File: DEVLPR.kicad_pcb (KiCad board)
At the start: 2 copper layers, 68.6 x 53.3 mm, 56 parts, among them CON1 3.5mm EMG, J1 EMG OUTPUT, P1 Power, P2 Analog, P3 Digital, P4 Digital, P5 CONN_01X01, P6 CONN_01X01, P7 CONN_01X01, P8 CONN_01X01, U1 TPS60402, U2 MAX1735, U3 OPA375DCK, U4 INA819IDGK, U5 OPA376xxD, U6 OPA376xxD

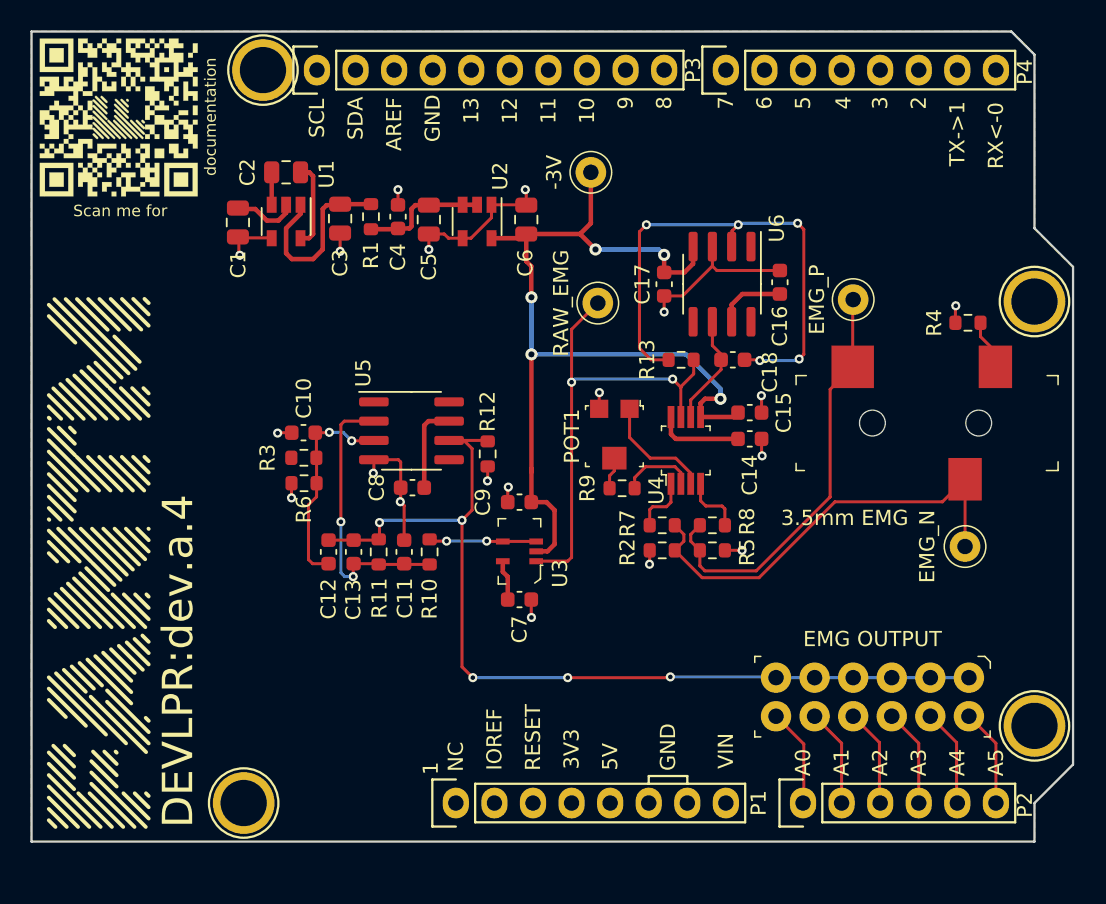
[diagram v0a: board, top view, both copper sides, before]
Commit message: Created v1.1 of the DEVLPR, adding RLD
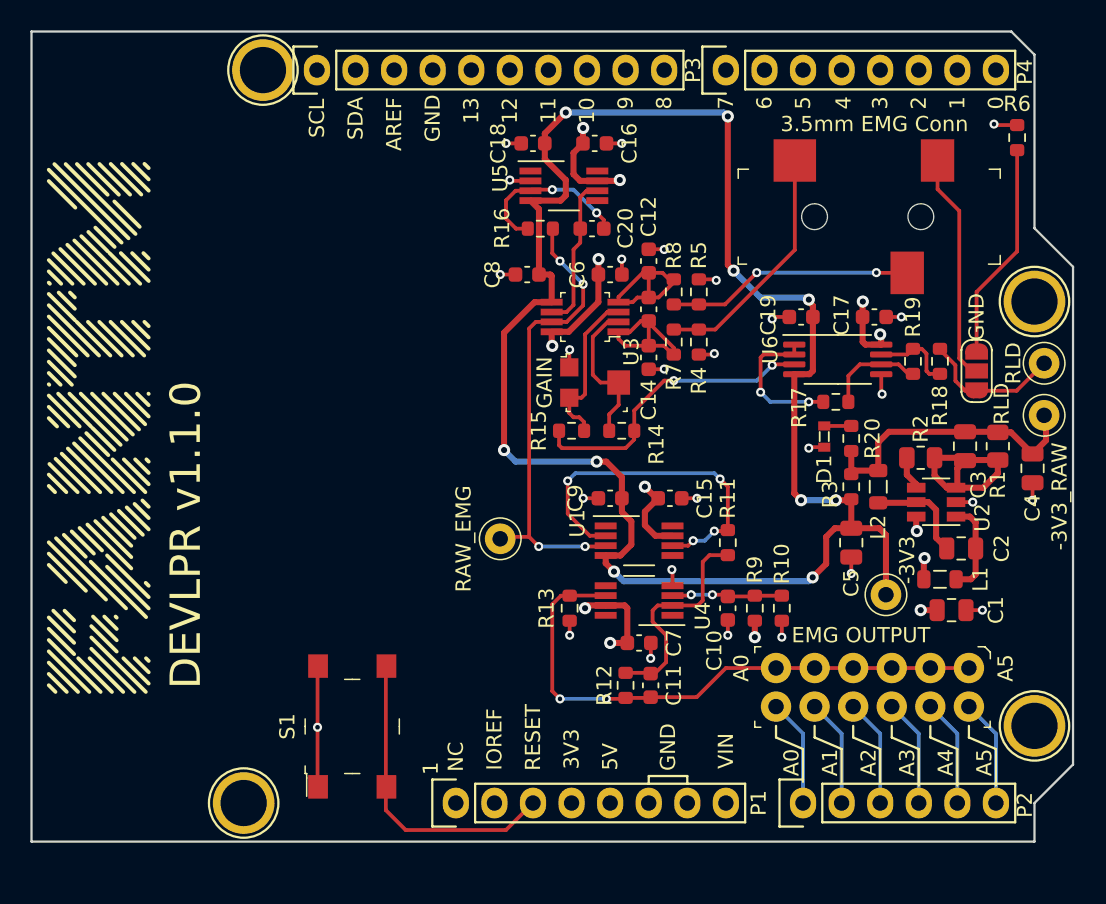
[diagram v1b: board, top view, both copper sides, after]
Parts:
- removed the C11 at (135.5, 107.3)
- removed the C6 at (143.6, 85.4)
- removed the C8 at (136.1, 103.1)
- removed G***: LOGO, kicad:oh_norm
- removed G***: LOGO, kicad:cc_reg
- removed G***: LOGO, kicad:logo
- removed the R4 at (172.7, 92.2)
- removed REF**: KiCad-Logo2_5mm_SilkScreen, Symbol:KiCad-Logo2_5mm_SilkScreen
- added C13: 10pF, Capacitor_SMD:C_0603_1608Metric, F.Cu at (151.6, 91.3)
- added C14: 2.2pF, Capacitor_SMD:C_0603_1608Metric, F.Cu at (151.6, 94.5)
- added C15: 0.1uF, Capacitor_SMD:C_0603_1608Metric, F.Cu at (153.0, 103.8)
- added C16: 0.1uF, Capacitor_SMD:C_0603_1608Metric, F.Cu at (148.1, 80.4)
- added C18: 0.1uF, Capacitor_SMD:C_0603_1608Metric, F.Cu at (144.0, 80.4)
- added D1: GREEN LED, digikey-footprints:0603, F.Cu at (163.2, 99.7)
- added JP1: RLD_SEL, Jumper:SolderJumper-3_P1.3mm_Open_RoundedPad1.0x1.5mm_NumberLabels, F.Cu at (173.2, 95.4)
- added L1: 10uH, Inductor_SMD:L_0805_2012Metric, F.Cu at (170.8, 109.1)
- added L2: 10uH, Inductor_SMD:L_0805_2012Metric, F.Cu at (166.8, 103.0)
- added R11: 10k, Resistor_SMD:R_0603_1608Metric, F.Cu at (156.8, 106.7)
- added R15: 470, Resistor_SMD:R_0603_1608Metric, F.Cu at (146.6, 99.3)
- added R17: 10k, Resistor_SMD:R_0603_1608Metric, F.Cu at (164.0, 97.4)
- added R18: 100k, Resistor_SMD:R_0603_1608Metric, F.Cu at (170.8, 94.7)
- added R19: 100k, Resistor_SMD:R_0603_1608Metric, F.Cu at (169.0, 94.7)
- added R2: 102k, Resistor_SMD:R_0805_2012Metric, F.Cu at (169.5, 101.1)
- added R20: 1k, Resistor_SMD:R_0603_1608Metric, F.Cu at (165.0, 99.8)
- added R3: 249, Resistor_SMD:R_0603_1608Metric, F.Cu at (165.0, 103.0)
- added S1: PTS645SM43SMTR92_LFS, digikey-footprints:Switch_Tactile_SMD_6x6mm_PTS645, F.Cu at (132.1, 118.8)
- added S2: Linus, FANTM:linus_xsm, B.Cu at (171.8, 109.0)
- added S3: Sinclair, FANTM:sin_ham_bitmap_sm, B.Cu at (172.9, 101.8)
- added S4: Kicad, Symbol:KiCad-Logo2_5mm_SilkScreen, B.Cu at (171.4, 84.3)
- added S5: OSHW, Symbol:OSHW-Symbol_6.7x6mm_SilkScreen, B.Cu at (171.4, 94.4)
- added S6: Portrait, FANTM:portait, B.Cu at (136.5, 80.9)
- added S7: Name, FANTM:name, B.Cu at (133.1, 116.0)
- C1, C2: value 3.3uF -> 1uF
- C12: value 4700pF -> 2.2pF
- C3: value 3.3uF -> 22pF
- C4: value 0.1uF -> 4.7uF; footprint Capacitor_SMD:C_0603_1608Metric -> Capacitor_SMD:C_0805_2012Metric
- C5: value 1uF -> 10uF
- CON1: value 3.5mm EMG -> SJ-3523-SMT-TR
- R1: value 249 -> 267k; footprint Resistor_SMD:R_0603_1608Metric -> Resistor_SMD:R_0805_2012Metric
- R10: value 3.3k -> 10k
- R12: renamed from R11; value 69.8k -> 28.7k
- R6: value 1k -> 100k
- R9: renamed from R3; value 43.2k -> 68k
- TP1: value EMG_N -> -3V3_RAW
- TP2: value EMG_P -> -3V3
- TP3: value -3V -> RAW_EMG
- TP4: value RAW_EMG -> RLD
- U1: value TPS60402 -> OPA187IDR; footprint Package_TO_SOT_SMD:SOT-23-5 -> Package_SO:VSSOP-8_3.0x3.0mm_P0.65mm
- U2: value MAX1735 -> LT3462A; footprint Package_TO_SOT_SMD:SOT-23-5 -> Package_TO_SOT_SMD:TSOT-23-6
- U3: value OPA375DCK -> INA821IDGKT; footprint digikey-footprints:SC-70-5 -> digikey-footprints:TSSOP-8_W3mm
- U4: value INA819IDGK -> OPA187IDR; footprint digikey-footprints:TSSOP-8_W3mm -> Package_SO:VSSOP-8_3.0x3.0mm_P0.65mm
- U5: value OPA376xxD -> OPA187IDR; footprint Package_SO:SOIC-8_3.9x4.9mm_P1.27mm -> Package_SO:VSSOP-8_3.0x3.0mm_P0.65mm
- U6: value OPA376xxD -> OPA2375IPWR; footprint Package_SO:SOIC-8_3.9x4.9mm_P1.27mm -> Package_SO:TSSOP-8_4.4x3mm_P0.65mm
- moved C1 53.5 mm to (171.6, 111.1), turned to 0 degrees
- moved R6 52.2 mm to (175.9, 80.0), turned to 90 degrees
- moved C2 50.9 mm to (172.2, 107.1)
- moved C4 44.9 mm to (176.9, 101.8)
- moved R1 44.0 mm to (174.6, 100.3), turned to 270 degrees
- moved C3 43.8 mm to (172.5, 100.3), turned to 270 degrees
- moved U2 35.4 mm to (170.6, 104.0), turned to 180 degrees
- moved C5 35.0 mm to (165.0, 106.7), turned to 270 degrees
- moved U1 31.3 mm to (151.0, 106.6), turned to 0 degrees
- moved R9 31.3 mm to (158.6, 111.0), turned to 90 degrees
- moved C10 30.2 mm to (156.8, 111.0), turned to 90 degrees
- moved TP4 29.7 mm to (177.7, 94.9)
- moved C12 28.5 mm to (151.6, 88.1)
- moved TP3 24.9 mm to (141.9, 106.4)
- moved R10 23.5 mm to (160.4, 111.0), turned to 270 degrees
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- renumbered C13 to C11, C16 to C17, C17 to C19, C18 to C20, C14 to C6, C15 to C8, R12 to R13, R9 to R14, R13 to R16, R2 to R4
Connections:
- C1 pad 1: GND -> +3V3
- C1 pad 2: +5V -> GND
- C11 pad 1: /EMG Amplifiers/BUFFER_OUT -> /EMG Amplifiers/BUFF_MID
- C12 pad 1: /EMG Amplifiers/V_SHIFT -> /EMG Amplifiers/INA_P
- C12 pad 2: /EMG_OUT -> GND
- C17 pad 2: +5V -> +3V3
- C19 pad 2: -3V -> -3V3
- C2 pad 1: /-5V Source/Cfly- -> /-3V3 Source/-3V3_D
- C2 pad 2: /-5V Source/Cfly+ -> /-3V3 Source/-3V3_SW
- C3 pad 1: GND -> /-3V3 Source/-3V3_RAW
- C3 pad 2: /-5V Source/INV_OUT -> /-3V3 Source/-3V3_FB
- C4 pad 1: GND -> /-3V3 Source/-3V3_RAW
- C4 pad 2: /-5V Source/LDO_IN -> GND
- C5 pad 1: GND -> -3V3
- C5 pad 2: /-5V Source/LDO_IN -> GND
- C6 pad 2: +5V -> +3V3
- C7 pad 2: +5V -> +3V3
- C8 pad 2: -3V -> -3V3
- C9 pad 2: -3V -> -3V3
- CON1 pad 2: /EMG_P -> /EMG_N
- CON1 pad 3: /EMG_N -> /EMG_P
- P1 pad 1: Net-(P1-Pad1) -> (no net)
- P1 pad 2: /IOREF -> (no net)
- P1 pad 5: +5V -> (no net)
- P1 pad 8: /Vin -> (no net)
- P3 pad 1: /SCL -> (no net)
- P3 pad 10: /8 -> (no net)
- P3 pad 2: /SDA -> (no net)
- P3 pad 3: /AREF -> (no net)
- P3 pad 5: /13(SCK) -> (no net)
- P3 pad 6: /12(SDI) -> (no net)
- P3 pad 7: /11(**|SDO) -> (no net)
- P3 pad 8: /10(**|CS) -> (no net)
- P3 pad 9: /9(**) -> (no net)
- P4 pad 1: /7 -> (no net)
- P4 pad 2: /6(**) -> (no net)
- P4 pad 3: /5(**) -> (no net)
- P4 pad 4: /4 -> (no net)
- P4 pad 5: /3(**) -> (no net)
- P4 pad 6: /2 -> (no net)
- P4 pad 7: /1(Tx) -> (no net)
- P4 pad 8: /0(Rx) -> (no net)
- P5 pad 1: Net-(P5-Pad1) -> (no net)
- P6 pad 1: Net-(P6-Pad1) -> (no net)
- P7 pad 1: Net-(P7-Pad1) -> (no net)
- P8 pad 1: Net-(P8-Pad1) -> (no net)
- POT1 pad 1: /EMG Amplifiers/RG_2 -> GND
- POT1 pad 2: Net-(POT1-Pad2) -> /EMG Amplifiers/RG1
- POT1 pad 3: GND -> /EMG Amplifiers/RG2
- R1 pad 1: /-5V Source/LDO_IN -> /-3V3 Source/-3V3_RAW
- R1 pad 2: /-5V Source/INV_OUT -> /-3V3 Source/-3V3_FB
- R10 pad 1: /EMG Amplifiers/BUFFER_OUT -> /EMG Amplifiers/V_SHIFT
- R10 pad 2: /EMG Amplifiers/BUFFER_FDBK -> GND
- R12 pad 2: /EMG Amplifiers/BUFFER_OUT -> /EMG Amplifiers/BUFF_MID
- R14 pad 1: Net-(POT1-Pad2) -> /EMG Amplifiers/RLD_IN
- R14 pad 2: /EMG Amplifiers/RG_1 -> /EMG Amplifiers/RG1
- R6 pad 1: /EMG Amplifiers/V_SHIFT -> /EMG Amplifiers/GND_REF
- R9 pad 1: +5V -> +3V3
- TP1 pad 1: /EMG_N -> /-3V3 Source/-3V3_RAW
- TP2 pad 1: /EMG_P -> -3V3
- TP3 pad 1: -3V -> /EMG Amplifiers/EMG_INSTR
- TP4 pad 1: /EMG Amplifiers/EMG_INSTR -> /EMG Amplifiers/RLD
- U1 pad 1: /-5V Source/INV_OUT -> (no net)
- U1 pad 2: +5V -> /EMG Amplifiers/BUFF_FDBK
- U1 pad 3: /-5V Source/Cfly- -> /EMG Amplifiers/EMG_INSTR
- U1 pad 4: GND -> -3V3
- U1 pad 5: /-5V Source/Cfly+ -> (no net)
- U2 pad 1: GND -> /-3V3 Source/-3V3_SW
- U2 pad 2: /-5V Source/LDO_IN -> GND
- U2 pad 3: /-5V Source/LDO_IN -> /-3V3 Source/-3V3_FB
- U2 pad 4: GND -> /-3V3 Source/-3V3_SDREF
- U2 pad 5: -3V -> /-3V3 Source/-3V3_D
- U3 pad 1: /EMG Amplifiers/EMG_INSTR -> /EMG Amplifiers/INA_N
- U3 pad 2: -3V -> /EMG Amplifiers/RG1
- U3 pad 3: /EMG Amplifiers/BUFFER_FDBK -> /EMG Amplifiers/RG2
- U3 pad 4: /EMG Amplifiers/BUFFER_FDBK -> /EMG Amplifiers/INA_P
- U3 pad 5: +5V -> -3V3
- U4 pad 1: /EMG Amplifiers/INA_N -> (no net)
- U4 pad 2: /EMG Amplifiers/RG_1 -> /EMG Amplifiers/BUFF_MID
- U4 pad 3: /EMG Amplifiers/RG_2 -> /EMG Amplifiers/V_SHIFT
- U4 pad 4: /EMG Amplifiers/INA_P -> GND
- U4 pad 5: -3V -> (no net)
- U4 pad 6: /EMG Amplifiers/INA_REF -> /EMG_OUT
- U4 pad 7: /EMG Amplifiers/EMG_INSTR -> +3V3
- U4 pad 8: +5V -> (no net)
- U5 pad 1: Net-(U5-Pad1) -> (no net)
- U5 pad 2: /EMG Amplifiers/BUFFER_OUT -> GND
- U5 pad 3: /EMG Amplifiers/V_SHIFT -> /EMG Amplifiers/REF_-
- U5 pad 4: GND -> -3V3
- U5 pad 5: Net-(U5-Pad5) -> (no net)
- U5 pad 6: /EMG_OUT -> /EMG Amplifiers/INA_REF
- U5 pad 7: +5V -> +3V3
- U5 pad 8: Net-(U5-Pad8) -> (no net)
- U6 pad 1: Net-(U6-Pad1) -> /EMG Amplifiers/RLD_MID
- U6 pad 2: /EMG Amplifiers/REF_- -> /EMG Amplifiers/RLD_MID
- U6 pad 3: GND -> /EMG Amplifiers/RLD_IN
- U6 pad 4: -3V -> -3V3
- U6 pad 5: Net-(U6-Pad5) -> GND
- U6 pad 6: /EMG Amplifiers/INA_REF -> /EMG Amplifiers/RLD_IN2_-
- U6 pad 7: +5V -> /EMG Amplifiers/RLD_OUT2
- U6 pad 8: Net-(U6-Pad8) -> +3V3
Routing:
- net -3V3: track 0.00 -> 116.4 mm, vias 0 -> 10
- net -3V: track 63.2 -> 0.00 mm, vias 5 -> 0
- net +3V3: track 0.00 -> 35.2 mm, vias 0 -> 13
- net /EMG_OUT: track 62.6 -> 38.0 mm, vias 5 -> 2
- net /EMG Amplifiers/REF_-: track 35.1 -> 11.0 mm, vias 5 -> 2
- net /EMG Amplifiers/BUFF_FDBK: track 0.00 -> 23.3 mm, vias 0 -> 4
- net +5V: track 22.9 -> 0.00 mm
- net /Reset: track 0.00 -> 20.4 mm
- net /EMG Amplifiers/RLD_IN: track 0.00 -> 19.9 mm, vias 0 -> 2
- net /-3V3 Source/-3V3_RAW: track 0.00 -> 19.3 mm
- net /EMG Amplifiers/BUFFER_OUT: track 19.1 -> 0.00 mm, vias 2 -> 0
- net /EMG Amplifiers/BUFF_MID: track 0.00 -> 14.7 mm
- net /EMG Amplifiers/GND_REF: track 0.00 -> 14.3 mm
- net /-3V3 Source/-3V3_FB: track 0.00 -> 13.2 mm
- net /EMG_N: track 29.1 -> 16.0 mm
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- added copper zone on In2.Cu, net +3V3
- added copper zone on In1.Cu, net GND
- removed copper zone on F.Cu, net +5V
- removed copper zone on B.Cu, net GND
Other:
- copper layers 2 -> 4
- net class Default: clearance 0 -> 0.1; trace_width 0.2 -> 0.25
- net class Power: clearance 0 -> 0.1; trace_width 0.3 -> 0.4
- rule trace_clearance: 0 -> 0.1
- board text added: "0"
- board text added: "DEVLPR v1.1.0"
- board text added: "Made with <3 by FANTM Ping hello@getfantm.com for support Check out docs.getfantm.com to get started"
- board text added: "Name:"
- board text added: "Portrait:"
- board text removed: ""Here, you learn what it is to be human. You are a creator of order, of beautiful shapes and systems, an organizer of chaos" -Dune"
- board text removed: "DEVLPR:dev.a.4"
- board text removed: "Made with <3 by FANTM Ping hello@getfantm.com for support"
- board text removed: "RX<-0"
- board text removed: "Scan me for"
- board text removed: "TX->1"
- board text removed: "documentation"
